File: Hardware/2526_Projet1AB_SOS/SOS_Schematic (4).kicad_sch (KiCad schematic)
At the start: 61 parts, among them J1 USB_C_Receptacle_USB2.0_16P, J2 Conn_ST_STDC14, SW1 SW_SPDT, SW2 SW_Push, SW3 SW_Push, SW4 SW_Push, SW5 SW_Push, U1 BU33SD5WG-TR, U2 USBLC6-2SC6, U3 STM32L476RGTx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

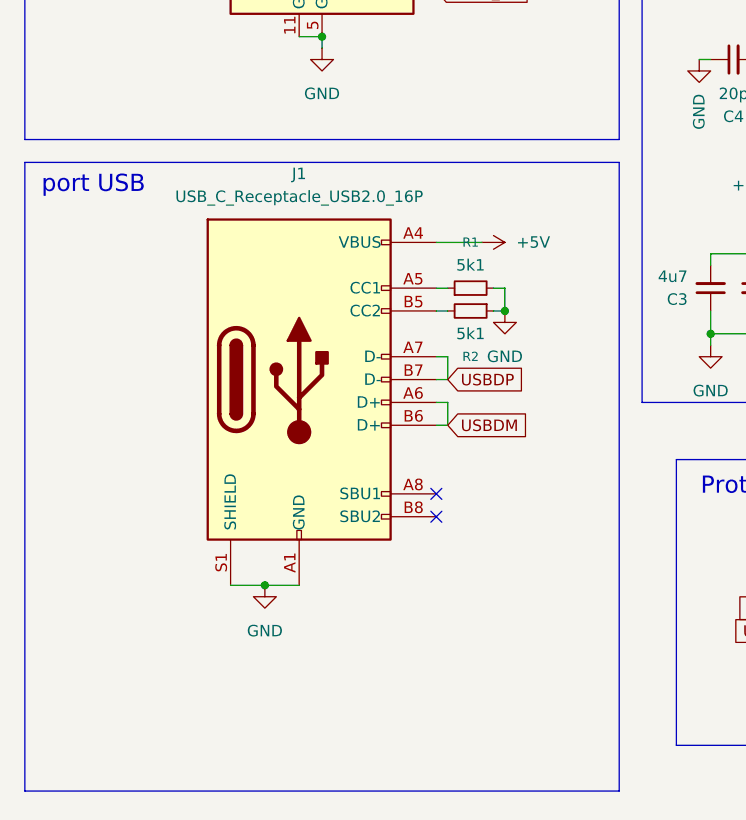
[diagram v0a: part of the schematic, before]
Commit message: USB and board routing
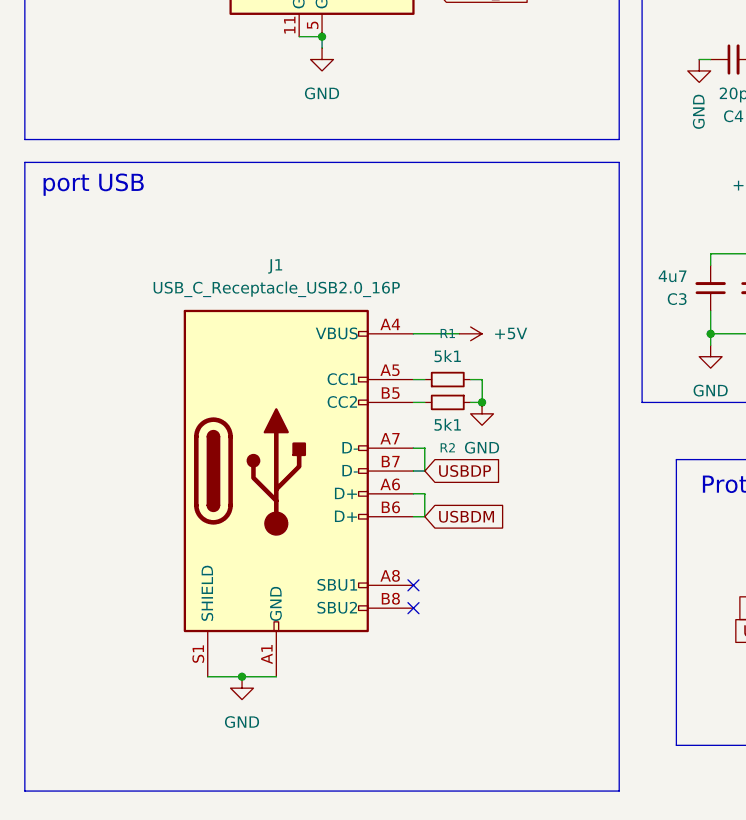
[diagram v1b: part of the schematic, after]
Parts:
- J1: footprint (none) -> Connector_USB:USB_C_Receptacle_GCT_USB4105-xx-A_16P_TopMnt_Horizontal
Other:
- moved on the sheet: J1, R1, R2
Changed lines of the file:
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@@
 	)
 	(junction
-		(at 40.64 171.45)
+		(at 38.1 181.61)
 		(diameter 0)
 		(color 0 0 0 0)
@@
 	)
 	(junction
-		(at 67.31 140.97)
+		(at 64.77 151.13)
 		(diameter 0)
 		(color 0 0 0 0)
@@
 	)
 	(no_connect
-		(at 59.69 161.29)
+		(at 57.15 171.45)
 	)
 	(no_connect
@@
 	)
 	(no_connect
-		(at 59.69 163.83)
+		(at 57.15 173.99)
 	)
 	(no_connect
@@
 	(wire
 		(pts
-			(xy 59.69 151.13) (xy 60.96 151.13)
+			(xy 57.15 161.29) (xy 58.42 161.29)
 		)
 		(stroke
@@
 	(wire
 		(pts
-			(xy 60.96 148.59) (xy 59.69 148.59)
+			(xy 58.42 158.75) (xy 57.15 158.75)
 		)
 		(stroke
@@
 	(wire
 		(pts
-			(xy 64.77 133.35) (xy 59.69 133.35)
+			(xy 62.23 143.51) (xy 57.15 143.51)
 		)
 		(stroke
@@
 	(wire
 		(pts
-			(xy 60.96 151.13) (xy 60.96 153.67)
+			(xy 58.42 161.29) (xy 58.42 163.83)
 		)
 		(stroke
@@
 	(wire
 		(pts
-			(xy 59.69 153.67) (xy 60.96 153.67)
+			(xy 57.15 163.83) (xy 58.42 163.83)
 		)
 		(stroke
@@
 	(wire
 		(pts
-			(xy 60.96 146.05) (xy 60.96 148.59)
+			(xy 58.42 156.21) (xy 58.42 158.75)
 		)
 		(stroke
@@
 	(wire
 		(pts
-			(xy 36.83 171.45) (xy 40.64 171.45)
+			(xy 34.29 181.61) (xy 38.1 181.61)
 		)
 		(stroke
@@
 	(wire
 		(pts
-			(xy 67.31 140.97) (xy 67.31 138.43)
+			(xy 64.77 151.13) (xy 64.77 148.59)
 		)
 		(stroke
@@
 	(wire
 		(pts
-			(xy 67.31 138.43) (xy 66.04 138.43)
+			(xy 64.77 148.59) (xy 63.5 148.59)
 		)
 		(stroke
@@
 	(wire
 		(pts
-			(xy 60.96 138.43) (xy 59.69 138.43)
+			(xy 58.42 148.59) (xy 57.15 148.59)
 		)
 		(stroke
@@
 	(wire
 		(pts
-			(xy 66.04 140.97) (xy 67.31 140.97)
+			(xy 63.5 151.13) (xy 64.77 151.13)
 		)
 		(stroke
@@
 	(wire
 		(pts
-			(xy 59.69 146.05) (xy 60.96 146.05)
+			(xy 57.15 156.21) (xy 58.42 156.21)
 		)
 		(stroke
@@
 	(wire
 		(pts
-			(xy 40.64 171.45) (xy 44.45 171.45)
+			(xy 38.1 181.61) (xy 41.91 181.61)
 		)
 		(stroke
@@
 	(wire
 		(pts
-			(xy 59.69 140.97) (xy 60.96 140.97)
+			(xy 57.15 151.13) (xy 58.42 151.13)
 		)
 		(stroke
@@
 	(global_label "USBDP"
 		(shape input)
-		(at 60.96 148.59 0)
+		(at 58.42 158.75 0)
 		(fields_autoplaced yes)
 		(effects
@@
 		)
 		(property "Intersheetrefs" "${INTERSHEET_REFS}"
-			(at 70.2952 148.59 0)
+			(at 67.7552 158.75 0)
 			(effects
 				(font
@@
 	(global_label "USBDM"
 		(shape input)
-		(at 60.96 153.67 0)
+		(at 58.42 163.83 0)
 		(fields_autoplaced yes)
 		(effects
@@
 		)
 		(property "Intersheetrefs" "${INTERSHEET_REFS}"
-			(at 70.4766 153.67 0)
+			(at 67.9366 163.83 0)
 			(effects
 				(font
@@
 	(symbol
 		(lib_id "Connector:USB_C_Receptacle_USB2.0_16P")
-		(at 44.45 148.59 0)
+		(at 41.91 158.75 0)
 		(unit 1)
 		(exclude_from_sim no)
@@
 		(fields_autoplaced yes)
 		(property "Reference" "J1"
-			(at 44.45 125.73 0)
+			(at 41.91 135.89 0)
 			(effects
 				(font
@@
 		)
 		(property "Value" "USB_C_Receptacle_USB2.0_16P"
-			(at 44.45 128.27 0)
+			(at 41.91 138.43 0)
 			(effects
 				(font
@@
 			)
 		)
-		(property "Footprint" ""
-			(at 48.26 148.59 0)
+		(property "Footprint" "Connector_USB:USB_C_Receptacle_GCT_USB4105-xx-A_16P_TopMnt_Horizontal"
+			(at 45.72 158.75 0)
 			(effects
 				(font
@@
 		)
 		(property "Datasheet" "https://www.usb.org/sites/default/files/documents/usb_type-c.zip"
-			(at 48.26 148.59 0)
+			(at 45.72 158.75 0)
 			(effects
 				(font
@@
 		)
 		(property "Description" "USB 2.0-only 16P Type-C Receptacle connector"
-			(at 44.45 148.59 0)
+			(at 41.91 158.75 0)
 			(effects
 				(font
@@
 	(symbol
 		(lib_id "power:GND")
-		(at 67.31 140.97 0)
+		(at 64.77 151.13 0)
 		(unit 1)
 		(exclude_from_sim no)
@@
 		(fields_autoplaced yes)
 		(property "Reference" "#PWR011"
-			(at 67.31 147.32 0)
+			(at 64.77 157.48 0)
 			(effects
 				(font
@@
 		)
 		(property "Value" "GND"
-			(at 67.31 146.05 0)
+			(at 64.77 156.21 0)
 			(effects
 				(font
@@
 		)
 		(property "Footprint" ""
-			(at 67.31 140.97 0)
+			(at 64.77 151.13 0)
 			(effects
 				(font
@@
 		)
 		(property "Datasheet" ""
-			(at 67.31 140.97 0)
+			(at 64.77 151.13 0)
 			(effects
 				(font
@@
 		)
 		(property "Description" "Power symbol creates a global label with name \"GND\" , ground"
-			(at 67.31 140.97 0)
+			(at 64.77 151.13 0)
 			(effects
 				(font
@@
 	(symbol
 		(lib_id "Device:R_Small")
-		(at 63.5 140.97 270)
+		(at 60.96 151.13 270)
 		(unit 1)
 		(exclude_from_sim no)
@@
 		(fields_autoplaced yes)
 		(property "Reference" "R2"
-			(at 63.5 146.05 90)
+			(at 60.96 156.21 90)
 			(effects
 				(font
@@
 		)
 		(property "Value" "5k1"
-			(at 63.5 143.51 90)
+			(at 60.96 153.67 90)
 			(effects
 				(font
@@
 		)
 		(property "Footprint" "Resistor_SMD:R_0603_1608Metric"
-			(at 63.5 140.97 0)
+			(at 60.96 151.13 0)
 			(effects
 				(font
@@
 		)
 		(property "Datasheet" "~"
-			(at 63.5 140.97 0)
+			(at 60.96 151.13 0)
 			(effects
 				(font
@@
 		)
 		(property "Description" "Resistor, small symbol"
-			(at 63.5 140.97 0)
+			(at 60.96 151.13 0)
 			(effects
 				(font
@@
 	(symbol
 		(lib_id "Device:R_Small")
-		(at 63.5 138.43 90)
+		(at 60.96 148.59 90)
 		(unit 1)
 		(exclude_from_sim no)
@@
 		(fields_autoplaced yes)
 		(property "Reference" "R1"
-			(at 63.5 133.35 90)
+			(at 60.96 143.51 90)
 			(effects
 				(font
@@
 		)
 		(property "Value" "5k1"
-			(at 63.5 135.89 90)
+			(at 60.96 146.05 90)
 			(effects
 				(font
@@
 		)
 		(property "Footprint" "Resistor_SMD:R_0603_1608Metric"
-			(at 63.5 138.43 0)
+			(at 60.96 148.59 0)
 			(effects
 				(font
@@
 		)
 		(property "Datasheet" "~"
-			(at 63.5 138.43 0)
+			(at 60.96 148.59 0)
 			(effects
 				(font
@@
 		)
 		(property "Description" "Resistor, small symbol"
-			(at 63.5 138.43 0)
+			(at 60.96 148.59 0)
 			(effects
 				(font
@@
 	(symbol
 		(lib_id "power:+5V")
-		(at 64.77 133.35 270)
+		(at 62.23 143.51 270)
 		(unit 1)
 		(exclude_from_sim no)
@@
 		(fields_autoplaced yes)
 		(property "Reference" "#PWR010"
-			(at 60.96 133.35 0)
+			(at 58.42 143.51 0)
 			(effects
 				(font
@@
 		)
 		(property "Value" "+5V"
-			(at 68.58 133.3499 90)
+			(at 66.04 143.5099 90)
 			(effects
 				(font
@@
 		)
 		(property "Footprint" ""
-			(at 64.77 133.35 0)
+			(at 62.23 143.51 0)
 			(effects
 				(font
@@
 		)
 		(property "Datasheet" ""
-			(at 64.77 133.35 0)
+			(at 62.23 143.51 0)
 			(effects
 				(font
@@
 		)
 		(property "Description" "Power symbol creates a global label with name \"+5V\""
-			(at 64.77 133.35 0)
+			(at 62.23 143.51 0)
 			(effects
 				(font
@@
 	(symbol
 		(lib_id "power:GND")
-		(at 40.64 171.45 0)
+		(at 38.1 181.61 0)
 		(unit 1)
 		(exclude_from_sim no)
@@
 		(fields_autoplaced yes)
 		(property "Reference" "#PWR03"
-			(at 40.64 177.8 0)
+			(at 38.1 187.96 0)
 			(effects
 				(font
@@
 		)
 		(property "Value" "GND"
-			(at 40.64 176.53 0)
+			(at 38.1 186.69 0)
 			(effects
 				(font
@@
 		)
 		(property "Footprint" ""
-			(at 40.64 171.45 0)
+			(at 38.1 181.61 0)
 			(effects
 				(font
@@
 		)
 		(property "Datasheet" ""
-			(at 40.64 171.45 0)
+			(at 38.1 181.61 0)
 			(effects
 				(font
@@
 		)
 		(property "Description" "Power symbol creates a global label with name \"GND\" , ground"
-			(at 40.64 171.45 0)
+			(at 38.1 181.61 0)
 			(effects
 				(font
